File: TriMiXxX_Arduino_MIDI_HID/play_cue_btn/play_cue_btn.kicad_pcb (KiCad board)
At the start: 2 copper layers, 77.8 x 39.4 mm, 36 parts, among them J1 PLAY_CUE, Q1 2N7000, Q2 2N7000, SW1 SW_PLAY, SW2 SW_CUE

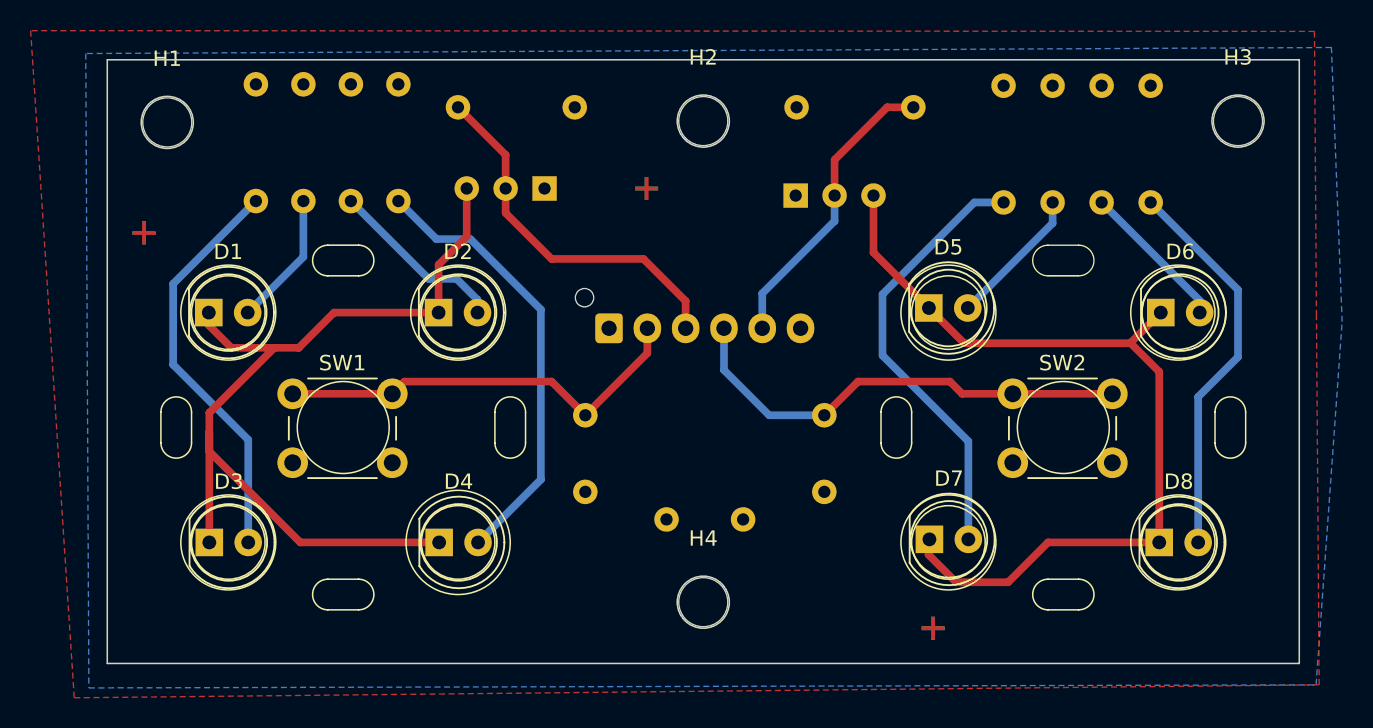
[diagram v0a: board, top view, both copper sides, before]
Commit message: Update schematics for jlcpcb productions, new dims, and sunlu petgcf calibration
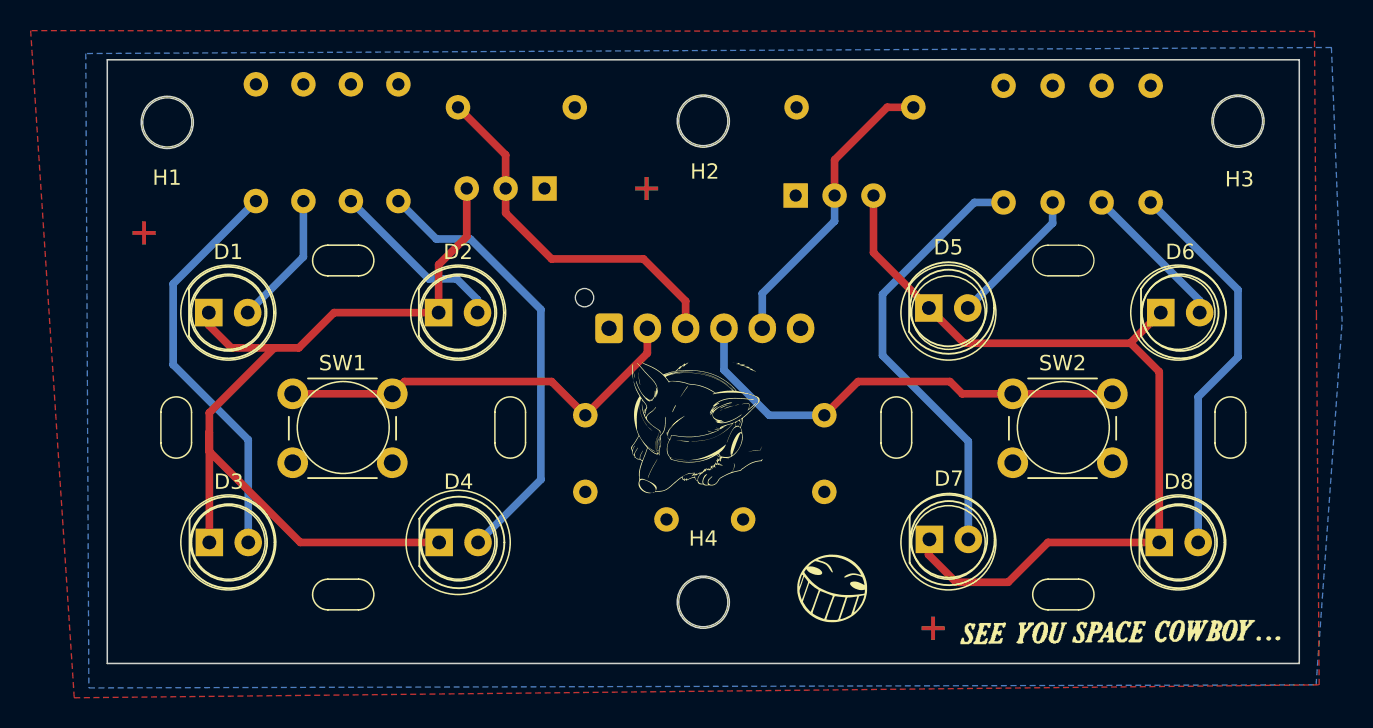
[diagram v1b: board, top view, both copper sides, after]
